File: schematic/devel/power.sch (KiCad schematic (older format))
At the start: 26 parts

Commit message: made small adjustments, created netlist
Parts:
- gave numbers to parts that had none: 26
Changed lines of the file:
@@
 P 1850 1850
 AR Path="/5D81CCCC" Ref="C?"  Part="1"
-AR Path="/5D7CE105/5D81CCCC" Ref="C?"  Part="1"
-F 0 "C?" H 1938 1896 50  0000 L CNN
+AR Path="/5D7CE105/5D81CCCC" Ref="C4"  Part="1"
+F 0 "C4" H 1938 1896 50  0000 L CNN
 F 1 "10u" H 1938 1805 50  0000 L CNN
 F 2 "" H 1850 1850 50  0001 C CNN
@@
 P 2300 1850
 AR Path="/5D81CCE9" Ref="C?"  Part="1"
-AR Path="/5D7CE105/5D81CCE9" Ref="C?"  Part="1"
-F 0 "C?" H 2388 1896 50  0000 L CNN
+AR Path="/5D7CE105/5D81CCE9" Ref="C6"  Part="1"
+F 0 "C6" H 2388 1896 50  0000 L CNN
 F 1 "1u" H 2388 1805 50  0000 L CNN
 F 2 "" H 2300 1850 50  0001 C CNN
@@
 P 2700 1150
 AR Path="/5D81CCF3" Ref="TP?"  Part="1"
-AR Path="/5D7CE105/5D81CCF3" Ref="TP?"  Part="1"
-F 0 "TP?" H 2642 1176 50  0000 R CNN
+AR Path="/5D7CE105/5D81CCF3" Ref="TP1"  Part="1"
+F 0 "TP1" H 2642 1176 50  0000 R CNN
 F 1 "TestPoint" H 2642 1267 50  0000 R CNN
 F 2 "" H 2900 1150 50  0001 C CNN
@@
 P 2700 1650
 AR Path="/5D81CCFC" Ref="TP?"  Part="1"
-AR Path="/5D7CE105/5D81CCFC" Ref="TP?"  Part="1"
-F 0 "TP?" H 2642 1676 50  0000 R CNN
+AR Path="/5D7CE105/5D81CCFC" Ref="TP2"  Part="1"
+F 0 "TP2" H 2642 1676 50  0000 R CNN
 F 1 "TestPoint" H 2642 1767 50  0000 R CNN
 F 2 "" H 2900 1650 50  0001 C CNN
@@
 P 2700 2150
 AR Path="/5D81CD05" Ref="TP?"  Part="1"
-AR Path="/5D7CE105/5D81CD05" Ref="TP?"  Part="1"
-F 0 "TP?" H 2642 2176 50  0000 R CNN
+AR Path="/5D7CE105/5D81CD05" Ref="TP3"  Part="1"
+F 0 "TP3" H 2642 2176 50  0000 R CNN
 F 1 "TestPoint" H 2642 2267 50  0000 R CNN
 F 2 "" H 2900 2150 50  0001 C CNN
@@
 P 950 1600
 AR Path="/5D81CD28" Ref="J?"  Part="1"
-AR Path="/5D7CE105/5D81CD28" Ref="J?"  Part="1"
-F 0 "J?" H 1000 1850 50  0000 C CNN
+AR Path="/5D7CE105/5D81CD28" Ref="J1"  Part="1"
+F 0 "J1" H 1000 1850 50  0000 C CNN
 F 1 "CONN_PWR" V 850 1600 50  0000 C CNN
 F 2 "" H 950 1600 50  0001 C CNN
@@
 P 3300 4800
 AR Path="/5D8917CB" Ref="TP?"  Part="1"
-AR Path="/5D7CE105/5D8917CB" Ref="TP?"  Part="1"
-F 0 "TP?" H 3242 4826 50  0000 R CNN
+AR Path="/5D7CE105/5D8917CB" Ref="TP5"  Part="1"
+F 0 "TP5" H 3242 4826 50  0000 R CNN
 F 1 "TestPoint" H 3242 4917 50  0000 R CNN
 F 2 "" H 3500 4800 50  0001 C CNN
@@
 P 3300 3800
 AR Path="/5D8917D4" Ref="TP?"  Part="1"
-AR Path="/5D7CE105/5D8917D4" Ref="TP?"  Part="1"
-F 0 "TP?" H 3242 3826 50  0000 R CNN
+AR Path="/5D7CE105/5D8917D4" Ref="TP4"  Part="1"
+F 0 "TP4" H 3242 3826 50  0000 R CNN
 F 1 "TestPoint" H 3242 3917 50  0000 R CNN
 F 2 "" H 3500 3800 50  0001 C CNN
@@
 P 7350 3750
 AR Path="/5D8917DB" Ref="TP?"  Part="1"
-AR Path="/5D7CE105/5D8917DB" Ref="TP?"  Part="1"
-F 0 "TP?" H 7292 3776 50  0000 R CNN
+AR Path="/5D7CE105/5D8917DB" Ref="TP6"  Part="1"
+F 0 "TP6" H 7292 3776 50  0000 R CNN
 F 1 "TestPoint" H 7292 3867 50  0000 R CNN
 F 2 "" H 7550 3750 50  0001 C CNN
@@
 P 6950 3850
 AR Path="/5D8917E7" Ref="R?"  Part="1"
-AR Path="/5D7CE105/5D8917E7" Ref="R?"  Part="1"
-F 0 "R?" H 7050 3900 50  0000 L CNN
+AR Path="/5D7CE105/5D8917E7" Ref="R1"  Part="1"
+F 0 "R1" H 7050 3900 50  0000 L CNN
 F 1 "100" H 7050 3800 50  0000 L CNN
 F 2 "" H 6950 3850 50  0001 C CNN
@@
 P 6950 4050
 AR Path="/5D8917ED" Ref="C?"  Part="1"
-AR Path="/5D7CE105/5D8917ED" Ref="C?"  Part="1"
-F 0 "C?" H 7042 4096 50  0000 L CNN
+AR Path="/5D7CE105/5D8917ED" Ref="C11"  Part="1"
+F 0 "C11" H 7042 4096 50  0000 L CNN
 F 1 "10n" H 7042 4005 50  0000 L CNN
 F 2 "" H 6950 4050 50  0001 C CNN
@@
 P 6500 3950
 AR Path="/5D8917FF" Ref="C?"  Part="1"
-AR Path="/5D7CE105/5D8917FF" Ref="C?"  Part="1"
-F 0 "C?" H 6592 3996 50  0000 L CNN
+AR Path="/5D7CE105/5D8917FF" Ref="C10"  Part="1"
+F 0 "C10" H 6592 3996 50  0000 L CNN
 F 1 "22u" H 6592 3905 50  0000 L CNN
 F 2 "" H 6500 3950 50  0001 C CNN
@@
 P 5850 3750
 AR Path="/5D891816" Ref="U?"  Part="1"
-AR Path="/5D7CE105/5D891816" Ref="U?"  Part="1"
-F 0 "U?" H 5850 4150 50  0000 C CNN
+AR Path="/5D7CE105/5D891816" Ref="U3"  Part="1"
+F 0 "U3" H 5850 4150 50  0000 C CNN
 F 1 "REF5010IDGK" H 6050 4050 50  0000 C CNN
 F 2 "Package_SO:MSOP-8_3x3mm_P0.65mm" H 5900 3500 50  0001 L CIN
@@
 P 1750 5150
 AR Path="/5D891822" Ref="D?"  Part="1"
-AR Path="/5D7CE105/5D891822" Ref="D?"  Part="1"
-F 0 "D?" H 1750 5000 50  0000 C CNN
+AR Path="/5D7CE105/5D891822" Ref="D2"  Part="1"
+F 0 "D2" H 1750 5000 50  0000 C CNN
 F 1 "1N4001" H 1750 4900 50  0000 C CNN
 F 2 "Diode_THT:D_DO-41_SOD81_P10.16mm_Horizontal" H 1750 4975 50  0001 C CNN
@@
 P 2800 4500
 AR Path="/5D89182E" Ref="D?"  Part="1"
-AR Path="/5D7CE105/5D89182E" Ref="D?"  Part="1"
-F 0 "D?" V 2846 4421 50  0000 R CNN
+AR Path="/5D7CE105/5D89182E" Ref="D4"  Part="1"
+F 0 "D4" V 2846 4421 50  0000 R CNN
 F 1 "1N4001" V 2755 4421 50  0000 R CNN
 F 2 "Diode_THT:D_DO-41_SOD81_P10.16mm_Horizontal" H 2800 4325 50  0001 C CNN
@@
 P 2800 4000
 AR Path="/5D89183A" Ref="D?"  Part="1"
-AR Path="/5D7CE105/5D89183A" Ref="D?"  Part="1"
-F 0 "D?" V 2754 4079 50  0000 L CNN
+AR Path="/5D7CE105/5D89183A" Ref="D3"  Part="1"
+F 0 "D3" V 2754 4079 50  0000 L CNN
 F 1 "1N4001" V 2845 4079 50  0000 L CNN
 F 2 "Diode_THT:D_DO-41_SOD81_P10.16mm_Horizontal" H 2800 3825 50  0001 C CNN
@@
 P 2300 4500
 AR Path="/5D89184B" Ref="C?"  Part="1"
-AR Path="/5D7CE105/5D89184B" Ref="C?"  Part="1"
-F 0 "C?" H 2388 4546 50  0000 L CNN
+AR Path="/5D7CE105/5D89184B" Ref="C8"  Part="1"
+F 0 "C8" H 2388 4546 50  0000 L CNN
 F 1 "1u" H 2388 4455 50  0000 L CNN
 F 2 "" H 2300 4500 50  0001 C CNN
@@
 P 2300 4000
 AR Path="/5D891851" Ref="C?"  Part="1"
-AR Path="/5D7CE105/5D891851" Ref="C?"  Part="1"
-F 0 "C?" H 2392 4046 50  0000 L CNN
+AR Path="/5D7CE105/5D891851" Ref="C7"  Part="1"
+F 0 "C7" H 2392 4046 50  0000 L CNN
 F 1 "100n" H 2392 3955 50  0000 L CNN
 F 2 "" H 2300 4000 50  0001 C CNN
@@
 P 1200 4500
 AR Path="/5D89185D" Ref="C?"  Part="1"
-AR Path="/5D7CE105/5D89185D" Ref="C?"  Part="1"
-F 0 "C?" H 1288 4546 50  0000 L CNN
+AR Path="/5D7CE105/5D89185D" Ref="C2"  Part="1"
+F 0 "C2" H 1288 4546 50  0000 L CNN
 F 1 "2.2u" H 1288 4455 50  0000 L CNN
 F 2 "" H 1200 4500 50  0001 C CNN
@@
 P 1200 4000
 AR Path="/5D891869" Ref="C?"  Part="1"
-AR Path="/5D7CE105/5D891869" Ref="C?"  Part="1"
-F 0 "C?" H 1292 4046 50  0000 L CNN
+AR Path="/5D7CE105/5D891869" Ref="C1"  Part="1"
+F 0 "C1" H 1292 4046 50  0000 L CNN
 F 1 "330n" H 1292 3955 50  0000 L CNN
 F 2 "" H 1200 4000 50  0001 C CNN
@@
 P 1750 4750
 AR Path="/5D891875" Ref="U?"  Part="1"
-AR Path="/5D7CE105/5D891875" Ref="U?"  Part="1"
-F 0 "U?" H 1750 4601 50  0000 C CNN
+AR Path="/5D7CE105/5D891875" Ref="U2"  Part="1"
+F 0 "U2" H 1750 4601 50  0000 C CNN
 F 1 "L7912" H 1750 4510 50  0000 C CNN
 F 2 "" H 1750 4550 50  0001 C CIN
@@
 P 1750 3750
 AR Path="/5D89187B" Ref="U?"  Part="1"
-AR Path="/5D7CE105/5D89187B" Ref="U?"  Part="1"
-F 0 "U?" H 1750 3992 50  0000 C CNN
+AR Path="/5D7CE105/5D89187B" Ref="U1"  Part="1"
+F 0 "U1" H 1750 3992 50  0000 C CNN
 F 1 "L7812" H 1750 3901 50  0000 C CNN
 F 2 "" H 1775 3600 50  0001 L CIN
@@
 P 4950 3800
 AR Path="/5D8918A1" Ref="C?"  Part="1"
-AR Path="/5D7CE105/5D8918A1" Ref="C?"  Part="1"
-F 0 "C?" H 5042 3846 50  0000 L CNN
+AR Path="/5D7CE105/5D8918A1" Ref="C9"  Part="1"
+F 0 "C9" H 5042 3846 50  0000 L CNN
 F 1 "330n" H 5042 3755 50  0000 L CNN
 F 2 "" H 4950 3800 50  0001 C CNN
@@
 P 1750 3350
 AR Path="/5D8918BC" Ref="D?"  Part="1"
-AR Path="/5D7CE105/5D8918BC" Ref="D?"  Part="1"
-F 0 "D?" H 1750 3566 50  0000 C CNN
+AR Path="/5D7CE105/5D8918BC" Ref="D1"  Part="1"
+F 0 "D1" H 1750 3566 50  0000 C CNN
 F 1 "1N4001" H 1750 3475 50  0000 C CNN
 F 2 "Diode_THT:D_DO-41_SOD81_P10.16mm_Horizontal" H 1750 3175 50  0001 C CNN
@@
 P 1850 1350
 AR Path="/5C9BC2C2" Ref="C?"  Part="1"
-AR Path="/5D7CE105/5C9BC2C2" Ref="C?"  Part="1"
-F 0 "C?" H 1938 1396 50  0000 L CNN
+AR Path="/5D7CE105/5C9BC2C2" Ref="C3"  Part="1"
+F 0 "C3" H 1938 1396 50  0000 L CNN
 F 1 "10u" H 1938 1305 50  0000 L CNN
 F 2 "" H 1850 1350 50  0001 C CNN
@@
 P 2300 1350
 AR Path="/5C9BC8E6" Ref="C?"  Part="1"
-AR Path="/5D7CE105/5C9BC8E6" Ref="C?"  Part="1"
-F 0 "C?" H 2388 1396 50  0000 L CNN
+AR Path="/5D7CE105/5C9BC8E6" Ref="C5"  Part="1"
+F 0 "C5" H 2388 1396 50  0000 L CNN
 F 1 "1u" H 2388 1305 50  0000 L CNN
 F 2 "" H 2300 1350 50  0001 C CNN

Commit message: assigned footprints to symbols
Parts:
- C1: footprint (none) -> Capacitor_SMD:C_0805_2012Metric
- C10: footprint (none) -> Capacitor_SMD:CP_Elec_5x5.4; symbol Device:C_Small -> Device:CP_Small
- C11: footprint (none) -> Capacitor_SMD:C_0402_1005Metric
- C2, C3, C4, C5, C6: footprint (none) -> Capacitor_SMD:CP_Elec_4x5.4
- C7, C9: footprint (none) -> Capacitor_SMD:C_0603_1608Metric
- C8: footprint (none) -> Capacitor_SMD:CP_Elec_5x4.4
- J1: footprint (none) -> Connector_PinHeader_1.00mm:PinHeader_1x03_P1.00mm_Vertical
- R1: footprint (none) -> Resistor_SMD:R_0603_1608Metric
- TP1, TP2, TP3, TP4, TP5, TP6: footprint (none) -> TestPoint:TestPoint_Bridge_Pitch2.54mm_Drill0.7mm
- U1, U2: footprint (none) -> Package_TO_SOT_SMD:TO-252-2
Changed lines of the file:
@@
 F 0 "C4" H 1938 1896 50  0000 L CNN
 F 1 "10u" H 1938 1805 50  0000 L CNN
-F 2 "" H 1850 1850 50  0001 C CNN
+F 2 "Capacitor_SMD:CP_Elec_4x5.4" H 1850 1850 50  0001 C CNN
 F 3 "~" H 1850 1850 50  0001 C CNN
 	1    1850 1850
@@
 F 0 "C6" H 2388 1896 50  0000 L CNN
 F 1 "1u" H 2388 1805 50  0000 L CNN
-F 2 "" H 2300 1850 50  0001 C CNN
+F 2 "Capacitor_SMD:CP_Elec_4x5.4" H 2300 1850 50  0001 C CNN
 F 3 "~" H 2300 1850 50  0001 C CNN
 	1    2300 1850
@@
 F 0 "TP1" H 2642 1176 50  0000 R CNN
 F 1 "TestPoint" H 2642 1267 50  0000 R CNN
-F 2 "" H 2900 1150 50  0001 C CNN
+F 2 "TestPoint:TestPoint_Bridge_Pitch2.54mm_Drill0.7mm" H 2900 1150 50  0001 C CNN
 F 3 "~" H 2900 1150 50  0001 C CNN
 	1    2700 1150
@@
 F 0 "TP2" H 2642 1676 50  0000 R CNN
 F 1 "TestPoint" H 2642 1767 50  0000 R CNN
-F 2 "" H 2900 1650 50  0001 C CNN
+F 2 "TestPoint:TestPoint_Bridge_Pitch2.54mm_Drill0.7mm" H 2900 1650 50  0001 C CNN
 F 3 "~" H 2900 1650 50  0001 C CNN
 	1    2700 1650
@@
 F 0 "TP3" H 2642 2176 50  0000 R CNN
 F 1 "TestPoint" H 2642 2267 50  0000 R CNN
-F 2 "" H 2900 2150 50  0001 C CNN
+F 2 "TestPoint:TestPoint_Bridge_Pitch2.54mm_Drill0.7mm" H 2900 2150 50  0001 C CNN
 F 3 "~" H 2900 2150 50  0001 C CNN
 	1    2700 2150
@@
 F 0 "J1" H 1000 1850 50  0000 C CNN
 F 1 "CONN_PWR" V 850 1600 50  0000 C CNN
-F 2 "" H 950 1600 50  0001 C CNN
+F 2 "Connector_PinHeader_1.00mm:PinHeader_1x03_P1.00mm_Vertical" H 950 1600 50  0001 C CNN
 F 3 "~" H 950 1600 50  0001 C CNN
 	1    950  1600
@@
 F 0 "TP5" H 3242 4826 50  0000 R CNN
 F 1 "TestPoint" H 3242 4917 50  0000 R CNN
-F 2 "" H 3500 4800 50  0001 C CNN
+F 2 "TestPoint:TestPoint_Bridge_Pitch2.54mm_Drill0.7mm" H 3500 4800 50  0001 C CNN
 F 3 "~" H 3500 4800 50  0001 C CNN
 	1    3300 4800
@@
 F 0 "TP4" H 3242 3826 50  0000 R CNN
 F 1 "TestPoint" H 3242 3917 50  0000 R CNN
-F 2 "" H 3500 3800 50  0001 C CNN
+F 2 "TestPoint:TestPoint_Bridge_Pitch2.54mm_Drill0.7mm" H 3500 3800 50  0001 C CNN
 F 3 "~" H 3500 3800 50  0001 C CNN
 	1    3300 3800
@@
 F 0 "TP6" H 7292 3776 50  0000 R CNN
 F 1 "TestPoint" H 7292 3867 50  0000 R CNN
-F 2 "" H 7550 3750 50  0001 C CNN
+F 2 "TestPoint:TestPoint_Bridge_Pitch2.54mm_Drill0.7mm" H 7550 3750 50  0001 C CNN
 F 3 "~" H 7550 3750 50  0001 C CNN
 	1    7350 3750
@@
 F 0 "R1" H 7050 3900 50  0000 L CNN
 F 1 "100" H 7050 3800 50  0000 L CNN
-F 2 "" H 6950 3850 50  0001 C CNN
+F 2 "Resistor_SMD:R_0603_1608Metric" H 6950 3850 50  0001 C CNN
 F 3 "~" H 6950 3850 50  0001 C CNN
 	1    6950 3850
@@
 F 0 "C11" H 7042 4096 50  0000 L CNN
 F 1 "10n" H 7042 4005 50  0000 L CNN
-F 2 "" H 6950 4050 50  0001 C CNN
+F 2 "Capacitor_SMD:C_0402_1005Metric" H 6950 4050 50  0001 C CNN
 F 3 "~" H 6950 4050 50  0001 C CNN
 	1    6950 4050
@@
 	6500 3850 6500 3650
 $Comp
-L Device:C_Small C?
+L Device:CP_Small C?
 U 1 1 5D8917FF
 P 6500 3950
@@
 F 0 "C10" H 6592 3996 50  0000 L CNN
 F 1 "22u" H 6592 3905 50  0000 L CNN
-F 2 "" H 6500 3950 50  0001 C CNN
+F 2 "Capacitor_SMD:CP_Elec_5x5.4" H 6500 3950 50  0001 C CNN
 F 3 "~" H 6500 3950 50  0001 C CNN
 	1    6500 3950
@@
 F 0 "C8" H 2388 4546 50  0000 L CNN
 F 1 "1u" H 2388 4455 50  0000 L CNN
-F 2 "" H 2300 4500 50  0001 C CNN
+F 2 "Capacitor_SMD:CP_Elec_5x4.4" H 2300 4500 50  0001 C CNN
 F 3 "~" H 2300 4500 50  0001 C CNN
 	1    2300 4500
@@
 F 0 "C7" H 2392 4046 50  0000 L CNN
 F 1 "100n" H 2392 3955 50  0000 L CNN
-F 2 "" H 2300 4000 50  0001 C CNN
+F 2 "Capacitor_SMD:C_0603_1608Metric" H 2300 4000 50  0001 C CNN
 F 3 "~" H 2300 4000 50  0001 C CNN
 	1    2300 4000
@@
 F 0 "C2" H 1288 4546 50  0000 L CNN
 F 1 "2.2u" H 1288 4455 50  0000 L CNN
-F 2 "" H 1200 4500 50  0001 C CNN
+F 2 "Capacitor_SMD:CP_Elec_4x5.4" H 1200 4500 50  0001 C CNN
 F 3 "~" H 1200 4500 50  0001 C CNN
 	1    1200 4500
@@
 F 0 "C1" H 1292 4046 50  0000 L CNN
 F 1 "330n" H 1292 3955 50  0000 L CNN
-F 2 "" H 1200 4000 50  0001 C CNN
+F 2 "Capacitor_SMD:C_0805_2012Metric" H 1200 4000 50  0001 C CNN
 F 3 "~" H 1200 4000 50  0001 C CNN
 	1    1200 4000
@@
 F 0 "U2" H 1750 4601 50  0000 C CNN
 F 1 "L7912" H 1750 4510 50  0000 C CNN
-F 2 "" H 1750 4550 50  0001 C CIN
+F 2 "Package_TO_SOT_SMD:TO-252-2" H 1750 4550 50  0001 C CIN
 F 3 "http://www.st.com/content/ccc/resource/technical/document/datasheet/c9/16/86/41/c7/2b/45/f2/CD00000450.pdf/files/CD00000450.pdf/jcr:content/translations/en.CD00000450.pdf" H 1750 4750 50  0001 C CNN
 	1    1750 4750
@@
 F 0 "U1" H 1750 3992 50  0000 C CNN
 F 1 "L7812" H 1750 3901 50  0000 C CNN
-F 2 "" H 1775 3600 50  0001 L CIN
+F 2 "Package_TO_SOT_SMD:TO-252-2" H 1775 3600 50  0001 L CIN
 F 3 "http://www.st.com/content/ccc/resource/technical/document/datasheet/41/4f/b3/b0/12/d4/47/88/CD00000444.pdf/files/CD00000444.pdf/jcr:content/translations/en.CD00000444.pdf" H 1750 3700 50  0001 C CNN
 	1    1750 3750
@@
 F 0 "C9" H 5042 3846 50  0000 L CNN
 F 1 "330n" H 5042 3755 50  0000 L CNN
-F 2 "" H 4950 3800 50  0001 C CNN
+F 2 "Capacitor_SMD:C_0603_1608Metric" H 4950 3800 50  0001 C CNN
 F 3 "~" H 4950 3800 50  0001 C CNN
 	1    4950 3800
@@
 F 0 "C3" H 1938 1396 50  0000 L CNN
 F 1 "10u" H 1938 1305 50  0000 L CNN
-F 2 "" H 1850 1350 50  0001 C CNN
+F 2 "Capacitor_SMD:CP_Elec_4x5.4" H 1850 1350 50  0001 C CNN
 F 3 "~" H 1850 1350 50  0001 C CNN
 	1    1850 1350
@@
 F 0 "C5" H 2388 1396 50  0000 L CNN
 F 1 "1u" H 2388 1305 50  0000 L CNN
-F 2 "" H 2300 1350 50  0001 C CNN
+F 2 "Capacitor_SMD:CP_Elec_4x5.4" H 2300 1350 50  0001 C CNN
 F 3 "~" H 2300 1350 50  0001 C CNN
 	1    2300 1350

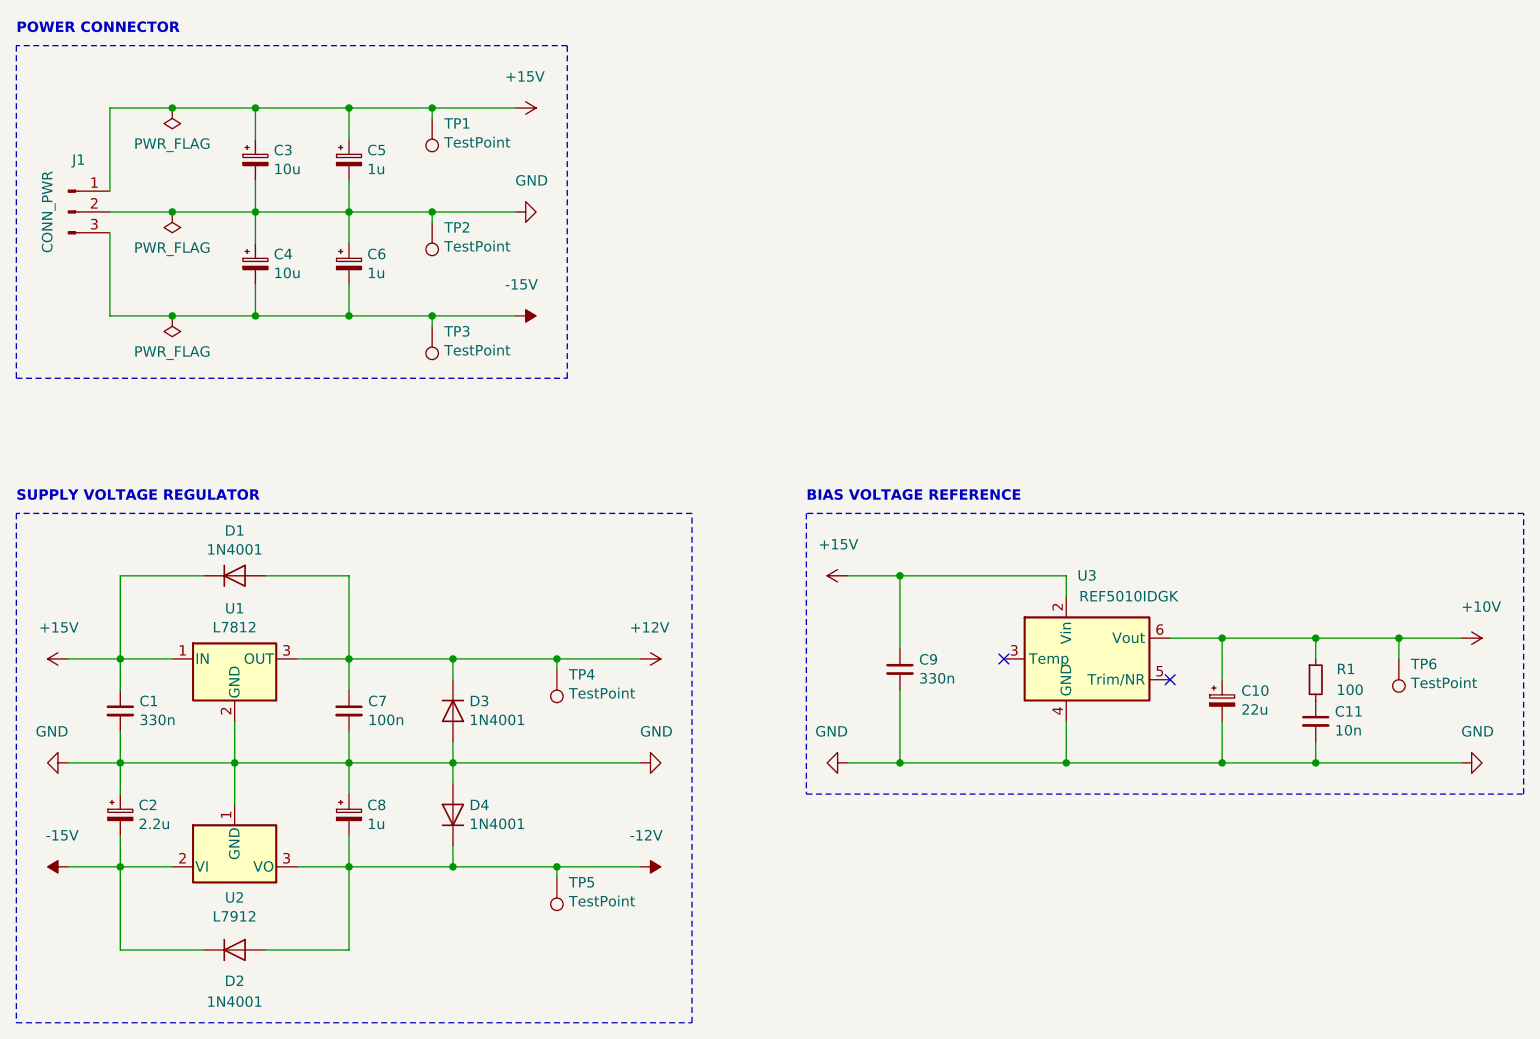
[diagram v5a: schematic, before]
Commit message: merged circuit sheets to single sheet, removed extra diodes, changed diode type
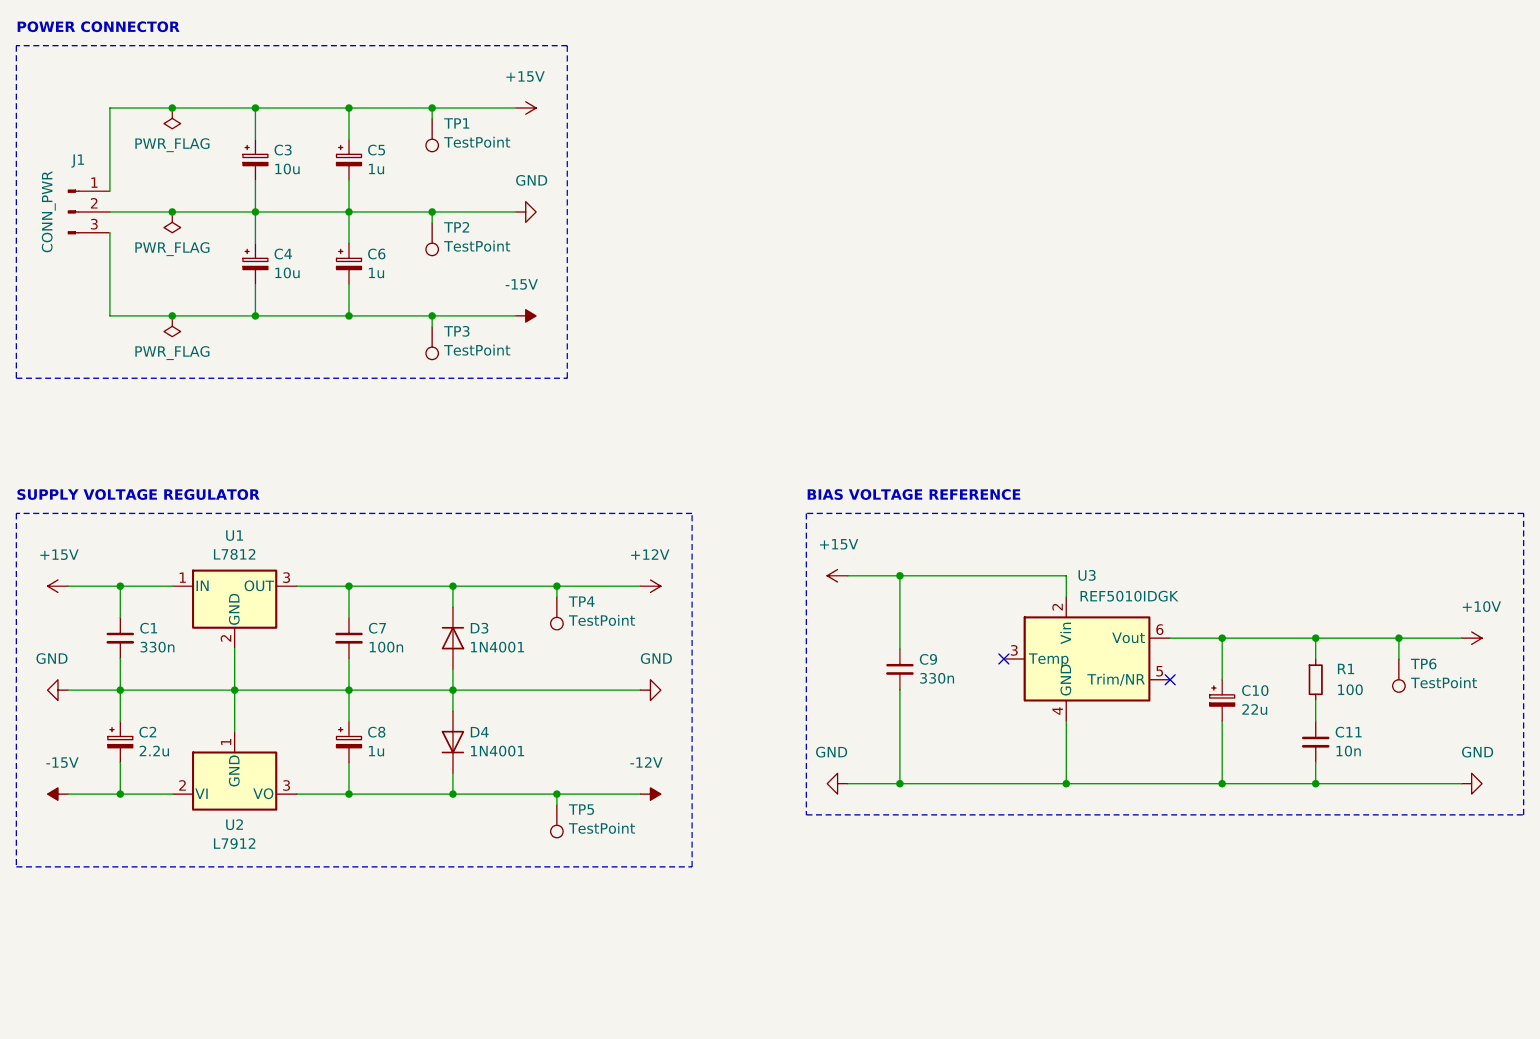
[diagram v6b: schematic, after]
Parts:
- removed D1, D2: 1N4001, Diode_THT:D_DO-41_SOD81_P10.16mm_Horizontal, symbol Diode:1N4001
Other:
- moved on the sheet: C1, C11, C2, C7, C8, D3, D4, TP4, TP5, U1, U2
